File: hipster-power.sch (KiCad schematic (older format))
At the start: 16 parts, among them SW3 ON|OFF, U3 NCP5501, U4 MCP73831

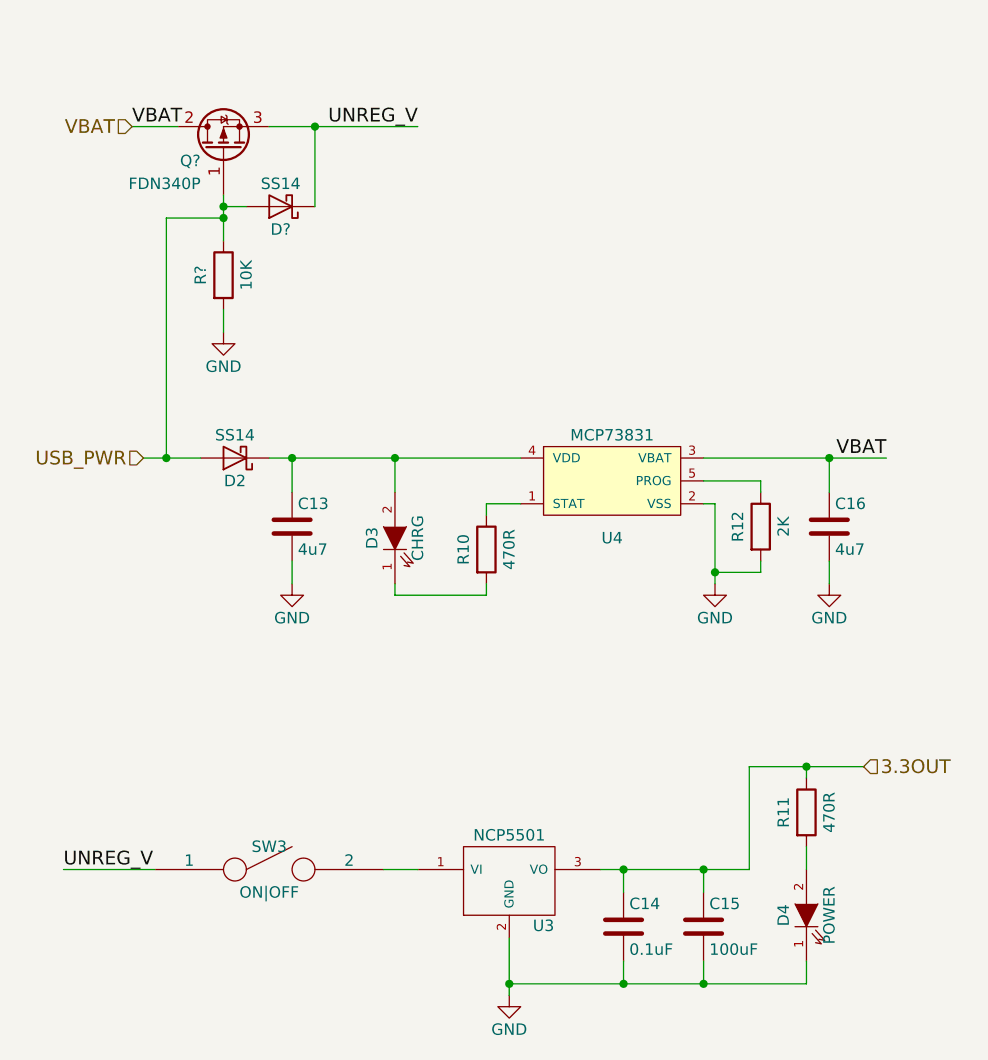
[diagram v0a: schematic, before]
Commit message: Remove power LED
Will reduce deep sleep power consumption to 1% or less of previous.

Ref #6.
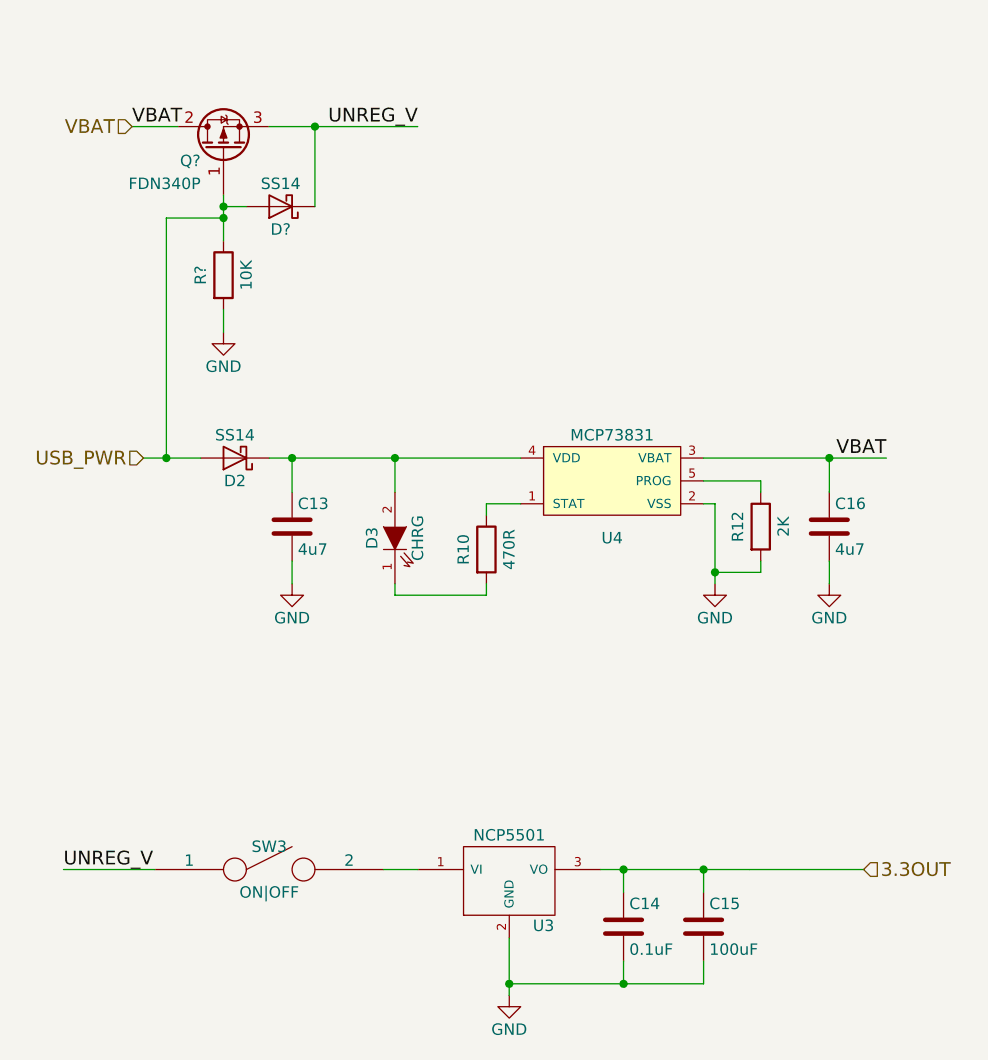
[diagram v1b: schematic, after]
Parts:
- removed D4: POWER, symbol LED-RESCUE-minimum-viable-badge
- removed R11: 470R, symbol R
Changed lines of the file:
@@
-$EndComp
-$Comp
-L LED-RESCUE-minimum-viable-badge D4
-U 1 1 59287320
-P 5200 4550
-AR Path="/59287320" Ref="D4"  Part="1"
-AR Path="/592826E7/59287320" Ref="D4"  Part="1"
-F 0 "D4" H 5200 4650 50  0000 C CNN
-F 1 "POWER" H 5200 4450 50  0000 C CNN
-F 2 "" H 5200 4550 50  0001 C CNN
-F 3 "" H 5200 4550 50  0000 C CNN
-	1    5200 4550
-	0    -1   -1   0
-$EndComp
-$Comp
-L R R11
-U 1 1 59287729
-P 5200 4100
-F 0 "R11" V 5100 4100 50  0000 C CNN
-F 1 "470R" V 5300 4100 50  0000 C CNN
-F 2 "" V 5130 4100 50  0001 C CNN
-F 3 "" H 5200 4100 50  0000 C CNN
-	1    5200 4100
-	1    0    0    -1
 $EndComp
 $Comp
@@
 	1    0    0    -1
 $EndComp
-Text HLabel 5450 3900 2    60   Input ~ 0
+Text HLabel 5450 4350 2    60   Input ~ 0
 3.3OUT
 $Comp
@@
 $EndComp
 Wire Wire Line
-	2300 2550 2550 2550
+	2300 2550 2400 2550
+Wire Wire Line
+	2400 2550 2550 2550
 Wire Wire Line
 	2950 3100 2950 3000
@@
 	3350 4350 3500 4350
 Wire Wire Line
-	5200 4350 5200 4250
-Wire Wire Line
-	4300 4350 4950 4350
-Wire Wire Line
-	4950 4350 4950 3900
-Wire Wire Line
-	4950 3900 5450 3900
-Wire Wire Line
-	5200 3900 5200 3950
+	4300 4350 4400 4350
+Wire Wire Line
+	4400 4350 4750 4350
+Wire Wire Line
+	4750 4350 4950 4350
+Wire Wire Line
+	4950 4350 4950 4350
+Wire Wire Line
+	4950 4350 5450 4350
 Wire Wire Line
 	4750 4450 4750 4350
@@
 Connection ~ 4400 4350
 Wire Wire Line
-	3900 4650 3900 4900
-Wire Wire Line
-	3900 4850 5200 4850
+	3900 4650 3900 4850
+Wire Wire Line
+	3900 4850 3900 4900
 Wire Wire Line
 	4400 4850 4400 4750
@@
 	4750 4850 4750 4750
 Connection ~ 4400 4850
-Wire Wire Line
-	5200 4850 5200 4750
-Connection ~ 4750 4850
 Connection ~ 3900 4850
-Connection ~ 5200 3900
-Wire Wire Line
-	2850 2550 3950 2550
+Wire Wire Line
+	2850 2550 2950 2550
+Wire Wire Line
+	2950 2550 3400 2550
+Wire Wire Line
+	3400 2550 3950 2550
 Wire Wire Line
 	3400 2700 3400 2550
@@
 	4750 2750 4800 2750
 Wire Wire Line
-	4800 2750 4800 3100
+	4800 2750 4800 3050
+Wire Wire Line
+	4800 3050 4800 3100
 Wire Wire Line
 	4800 3050 5000 3050
@@
 	5300 3100 5300 3000
 Wire Wire Line
-	4750 2550 5550 2550
+	4750 2550 5300 2550
+Wire Wire Line
+	5300 2550 5550 2550
 Wire Wire Line
 	5300 2550 5300 2700
@@
 	2250 1100 2450 1100
 Wire Wire Line
-	2850 1100 3500 1100
-Wire Wire Line
-	2650 1400 2650 1600
+	2850 1100 3050 1100
+Wire Wire Line
+	3050 1100 3500 1100
+Wire Wire Line
+	2650 1400 2650 1450
+Wire Wire Line
+	2650 1450 2650 1500
+Wire Wire Line
+	2650 1500 2650 1600
 Wire Wire Line
 	3050 1450 3050 1100
@@
 Wire Wire Line
 	2400 1500 2400 2550
+Wire Wire Line
+	4750 4850 4400 4850
+Wire Wire Line
+	4400 4850 3900 4850
 $EndSCHEMATC

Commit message: Arrange & label schematic, pass ERC
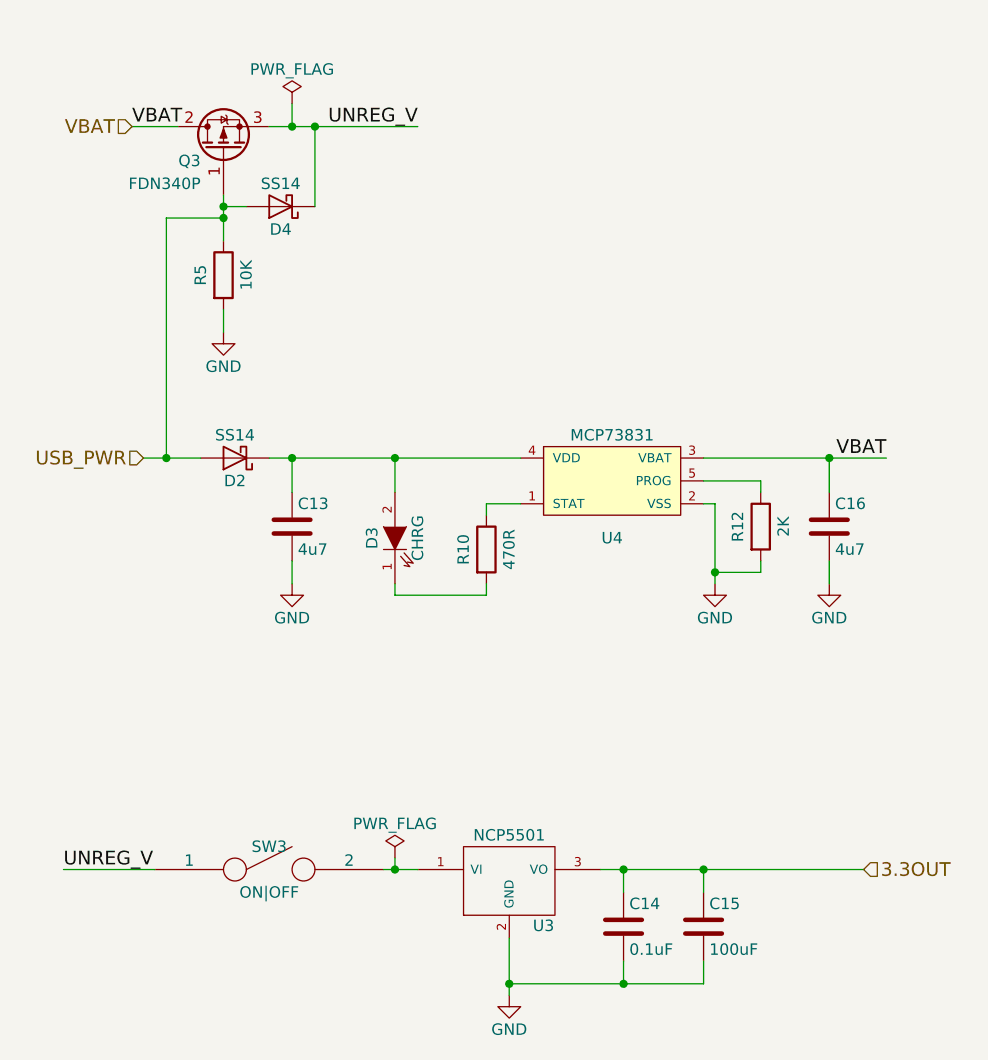
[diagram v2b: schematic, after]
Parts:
- gave numbers to parts that had none: 3
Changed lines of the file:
@@
 $Descr A4 11693 8268
 encoding utf-8
-Sheet 2 2
+Sheet 2 3
 Title ""
 Date ""
@@
 $EndComp
 $Comp
-L GND #PWR21
+L GND #PWR020
 U 1 1 592830E1
 P 2950 3100
-F 0 "#PWR21" H 2950 2850 50  0001 C CNN
+F 0 "#PWR020" H 2950 2850 50  0001 C CNN
 F 1 "GND" H 2950 2950 50  0000 C CNN
 F 2 "" H 2950 3100 50  0000 C CNN
@@
 $EndComp
 $Comp
-L GND #PWR22
+L GND #PWR021
 U 1 1 59287D1C
 P 3900 4900
-F 0 "#PWR22" H 3900 4650 50  0001 C CNN
+F 0 "#PWR021" H 3900 4650 50  0001 C CNN
 F 1 "GND" H 3900 4750 50  0000 C CNN
 F 2 "" H 3900 4900 50  0000 C CNN
@@
 $EndComp
 $Comp
-L GND #PWR23
+L GND #PWR022
 U 1 1 59358631
 P 4800 3100
-F 0 "#PWR23" H 4800 2850 50  0001 C CNN
+F 0 "#PWR022" H 4800 2850 50  0001 C CNN
 F 1 "GND" H 4800 2950 50  0000 C CNN
 F 2 "" H 4800 3100 50  0000 C CNN
@@
 $EndComp
 $Comp
-L GND #PWR24
+L GND #PWR023
 U 1 1 5935870E
 P 5300 3100
-F 0 "#PWR24" H 5300 2850 50  0001 C CNN
+F 0 "#PWR023" H 5300 2850 50  0001 C CNN
 F 1 "GND" H 5300 2950 50  0000 C CNN
 F 2 "" H 5300 3100 50  0000 C CNN
@@
 VBAT
 $Comp
-L D_Schottky D?
+L D_Schottky D4
 U 1 1 59A10ECB
 P 2900 1450
-F 0 "D?" H 2900 1550 50  0000 C CNN
+F 0 "D4" H 2900 1550 50  0000 C CNN
 F 1 "SS14" H 2900 1350 50  0000 C CNN
 F 2 "Diodes_SMD:D_SMA" H 2900 1450 50  0001 C CNN
@@
 $EndComp
 $Comp
-L GND #PWR?
+L GND #PWR024
 U 1 1 59A1135B
 P 2650 2000
-F 0 "#PWR?" H 2650 1750 50  0001 C CNN
+F 0 "#PWR024" H 2650 1750 50  0001 C CNN
 F 1 "GND" H 2650 1850 50  0000 C CNN
 F 2 "" H 2650 2000 50  0000 C CNN
@@
 $EndComp
 $Comp
-L R R?
+L R R5
 U 1 1 59A11654
 P 2650 1750
-F 0 "R?" V 2550 1750 50  0000 C CNN
+F 0 "R5" V 2550 1750 50  0000 C CNN
 F 1 "10K" V 2750 1750 50  0000 C CNN
 F 2 "" V 2580 1750 50  0001 C CNN
@@
 VBAT
 $Comp
-L Q_PMOS_GDS Q?
+L Q_PMOS_GDS Q3
 U 1 1 59A3FE7A
 P 2650 1200
-F 0 "Q?" V 2600 1300 50  0000 L CNN
+F 0 "Q3" V 2600 1300 50  0000 L CNN
 F 1 "FDN340P" V 2500 1300 50  0000 L CNN
 F 2 "" H 2850 1300 50  0001 C CNN
@@
 $EndComp
 Wire Wire Line
-	2300 2550 2400 2550
-Wire Wire Line
-	2400 2550 2550 2550
+	2300 2550 2550 2550
 Wire Wire Line
 	2950 3100 2950 3000
@@
 	3350 4350 3500 4350
 Wire Wire Line
-	4300 4350 4400 4350
-Wire Wire Line
-	4400 4350 4750 4350
-Wire Wire Line
-	4750 4350 4950 4350
-Wire Wire Line
-	4950 4350 4950 4350
-Wire Wire Line
-	4950 4350 5450 4350
+	4300 4350 5450 4350
 Wire Wire Line
 	4750 4450 4750 4350
@@
 Connection ~ 4400 4350
 Wire Wire Line
-	3900 4650 3900 4850
-Wire Wire Line
-	3900 4850 3900 4900
+	3900 4650 3900 4900
 Wire Wire Line
 	4400 4850 4400 4750
@@
 Connection ~ 3900 4850
 Wire Wire Line
-	2850 2550 2950 2550
-Wire Wire Line
-	2950 2550 3400 2550
-Wire Wire Line
-	3400 2550 3950 2550
+	2850 2550 3950 2550
 Wire Wire Line
 	3400 2700 3400 2550
@@
 	4750 2750 4800 2750
 Wire Wire Line
-	4800 2750 4800 3050
-Wire Wire Line
-	4800 3050 4800 3100
+	4800 2750 4800 3100
 Wire Wire Line
 	4800 3050 5000 3050
@@
 	5300 3100 5300 3000
 Wire Wire Line
-	4750 2550 5300 2550
-Wire Wire Line
-	5300 2550 5550 2550
+	4750 2550 5550 2550
 Wire Wire Line
 	5300 2550 5300 2700
@@
 	2250 1100 2450 1100
 Wire Wire Line
-	2850 1100 3050 1100
-Wire Wire Line
-	3050 1100 3500 1100
-Wire Wire Line
-	2650 1400 2650 1450
-Wire Wire Line
-	2650 1450 2650 1500
-Wire Wire Line
-	2650 1500 2650 1600
+	2850 1100 3500 1100
+Wire Wire Line
+	2650 1400 2650 1600
 Wire Wire Line
 	3050 1450 3050 1100
@@
 	2400 1500 2400 2550
 Wire Wire Line
-	4750 4850 4400 4850
-Wire Wire Line
-	4400 4850 3900 4850
+	3900 4850 4750 4850
+$Comp
+L PWR_FLAG #FLG025
+U 1 1 59A7D662
+P 3400 4300
+F 0 "#FLG025" H 3400 4375 50  0001 C CNN
+F 1 "PWR_FLAG" H 3400 4450 50  0000 C CNN
+F 2 "" H 3400 4300 50  0001 C CNN
+F 3 "" H 3400 4300 50  0001 C CNN
+	1    3400 4300
+	1    0    0    -1
+$EndComp
+Wire Wire Line
+	3400 4300 3400 4350
+Connection ~ 3400 4350
+$Comp
+L PWR_FLAG #FLG026
+U 1 1 59A7D985
+P 2950 1000
+F 0 "#FLG026" H 2950 1075 50  0001 C CNN
+F 1 "PWR_FLAG" H 2950 1150 50  0000 C CNN
+F 2 "" H 2950 1000 50  0001 C CNN
+F 3 "" H 2950 1000 50  0001 C CNN
+	1    2950 1000
+	1    0    0    -1
+$EndComp
+Wire Wire Line
+	2950 1000 2950 1100
+Connection ~ 2950 1100
 $EndSCHEMATC

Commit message: Add e-ink gate drive circuitry
Closes #14
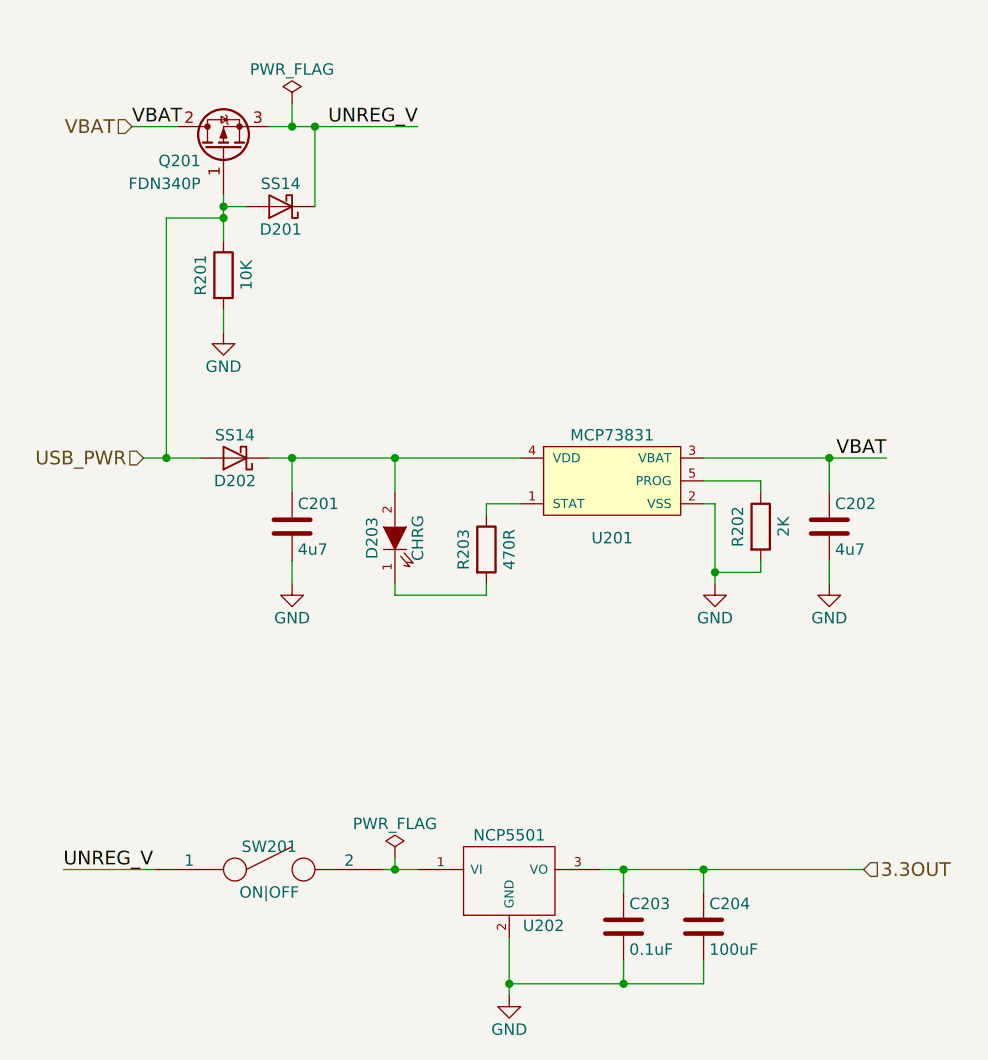
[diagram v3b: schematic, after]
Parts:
- renumbered C13 to C201, C16 to C202, C14 to C203, C15 to C204, D4 to D201, D2 to D202, D3 to D203, Q3 to Q201, R5 to R201, R12 to R202, R10 to R203, SW3 to SW201, U4 to U201, U3 to U202
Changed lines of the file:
@@
 USB_PWR
 $Comp
-L R R10
+L R R203
 U 1 1 59282A8D
 P 3800 2950
-F 0 "R10" V 3700 2950 50  0000 C CNN
+F 0 "R203" V 3700 2950 50  0000 C CNN
 F 1 "470R" V 3900 2950 50  0000 C CNN
 F 2 "Resistors_SMD:R_0603_HandSoldering" V 3730 2950 50  0001 C CNN
@@
 $EndComp
 $Comp
-L LED-RESCUE-minimum-viable-badge D3
+L LED-RESCUE-minimum-viable-badge D203
 U 1 1 59282B08
 P 3400 2900
-AR Path="/59282B08" Ref="D3"  Part="1"
-AR Path="/592826E7/59282B08" Ref="D3"  Part="1"
-F 0 "D3" H 3400 3000 50  0000 C CNN
+F 0 "D203" H 3400 3000 50  0000 C CNN
 F 1 "CHRG" H 3400 2800 50  0000 C CNN
 F 2 "LEDs:LED_0603" H 3400 2900 50  0001 C CNN
@@
 $EndComp
 $Comp
-L C C13
+L C C201
 U 1 1 59282FCC
 P 2950 2850
-F 0 "C13" H 2975 2950 50  0000 L CNN
+F 0 "C201" H 2975 2950 50  0000 L CNN
 F 1 "4u7" H 2975 2750 50  0000 L CNN
 F 2 "Capacitors_SMD:C_0805_HandSoldering" H 2988 2700 50  0001 C CNN
@@
 $EndComp
 $Comp
-L R R12
+L R R202
 U 1 1 592833D5
 P 5000 2850
-F 0 "R12" V 4900 2850 50  0000 C CNN
+F 0 "R202" V 4900 2850 50  0000 C CNN
 F 1 "2K" V 5100 2850 50  0000 C CNN
 F 2 "Resistors_SMD:R_0603_HandSoldering" V 4930 2850 50  0001 C CNN
@@
 UNREG_V
 $Comp
-L SPST SW3
+L SPST SW201
 U 1 1 59286658
 P 2850 4350
-F 0 "SW3" H 2850 4450 50  0000 C CNN
+F 0 "SW201" H 2850 4450 50  0000 C CNN
 F 1 "ON|OFF" H 2850 4250 50  0000 C CNN
 F 2 "libs:SS12D00" H 2850 4350 50  0001 C CNN
@@
 UNREG_V
 $Comp
-L NCP5501 U3
+L NCP5501 U202
 U 1 1 59286CBF
 P 3900 4400
-F 0 "U3" H 4050 4204 50  0000 C CNN
+F 0 "U202" H 4050 4204 50  0000 C CNN
 F 1 "NCP5501" H 3900 4600 50  0000 C CNN
 F 2 "libs:DPAK3.NCP5501" H 3900 4400 50  0001 C CNN
@@
 $EndComp
 $Comp
-L C C14
+L C C203
 U 1 1 59287000
 P 4400 4600
-F 0 "C14" H 4425 4700 50  0000 L CNN
+F 0 "C203" H 4425 4700 50  0000 L CNN
 F 1 "0.1uF" H 4425 4500 50  0000 L CNN
 F 2 "Capacitors_SMD:C_0603_HandSoldering" H 4438 4450 50  0001 C CNN
@@
 $EndComp
 $Comp
-L C C15
+L C C204
 U 1 1 592871C6
 P 4750 4600
-F 0 "C15" H 4775 4700 50  0000 L CNN
+F 0 "C204" H 4775 4700 50  0000 L CNN
 F 1 "100uF" H 4775 4500 50  0000 L CNN
 F 2 "Capacitors_SMD:C_1210_HandSoldering" H 4788 4450 50  0001 C CNN
@@
 3.3OUT
 $Comp
-L MCP73831 U4
+L MCP73831 U201
 U 1 1 5935729B
 P 4350 2650
-F 0 "U4" H 4350 2400 50  0000 C CNN
+F 0 "U201" H 4350 2400 50  0000 C CNN
 F 1 "MCP73831" H 4350 2850 50  0000 C CNN
 F 2 "TO_SOT_Packages_SMD:SOT-23-5_HandSoldering" H 4350 2650 60  0001 C CNN
@@
 $EndComp
 $Comp
-L C C16
+L C C202
 U 1 1 59358708
 P 5300 2850
-F 0 "C16" H 5325 2950 50  0000 L CNN
+F 0 "C202" H 5325 2950 50  0000 L CNN
 F 1 "4u7" H 5325 2750 50  0000 L CNN
 F 2 "Capacitors_SMD:C_0805_HandSoldering" H 5338 2700 50  0001 C CNN
@@
 VBAT
 $Comp
-L D_Schottky D4
+L D_Schottky D201
 U 1 1 59A10ECB
 P 2900 1450
-F 0 "D4" H 2900 1550 50  0000 C CNN
+F 0 "D201" H 2900 1550 50  0000 C CNN
 F 1 "SS14" H 2900 1350 50  0000 C CNN
 F 2 "Diodes_SMD:D_SMA" H 2900 1450 50  0001 C CNN
@@
 $EndComp
 $Comp
-L R R5
+L R R201
 U 1 1 59A11654
 P 2650 1750
-F 0 "R5" V 2550 1750 50  0000 C CNN
+F 0 "R201" V 2550 1750 50  0000 C CNN
 F 1 "10K" V 2750 1750 50  0000 C CNN
 F 2 "" V 2580 1750 50  0001 C CNN
@@
 VBAT
 $Comp
-L Q_PMOS_GDS Q3
+L Q_PMOS_GDS Q201
 U 1 1 59A3FE7A
 P 2650 1200
-F 0 "Q3" V 2600 1300 50  0000 L CNN
+F 0 "Q201" V 2600 1300 50  0000 L CNN
 F 1 "FDN340P" V 2500 1300 50  0000 L CNN
 F 2 "" H 2850 1300 50  0001 C CNN
@@
 Connection ~ 2650 1450
 $Comp
-L D_Schottky D2
+L D_Schottky D202
 U 1 1 592829A1
 P 2700 2550
-F 0 "D2" H 2700 2650 50  0000 C CNN
+F 0 "D202" H 2700 2650 50  0000 C CNN
 F 1 "SS14" H 2700 2450 50  0000 C CNN
 F 2 "Diodes_SMD:D_SMA" H 2700 2550 50  0001 C CNN

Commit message: Set component footprints.
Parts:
- Q201: footprint (none) -> libs:SOT23_FET
- R201: footprint (none) -> Resistors_SMD:R_0603_HandSoldering
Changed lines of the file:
@@
 F 0 "R201" V 2550 1750 50  0000 C CNN
 F 1 "10K" V 2750 1750 50  0000 C CNN
-F 2 "" V 2580 1750 50  0001 C CNN
+F 2 "Resistors_SMD:R_0603_HandSoldering" V 2580 1750 50  0001 C CNN
 F 3 "" H 2650 1750 50  0000 C CNN
 	1    2650 1750
@@
 F 0 "Q201" V 2600 1300 50  0000 L CNN
 F 1 "FDN340P" V 2500 1300 50  0000 L CNN
-F 2 "" H 2850 1300 50  0001 C CNN
+F 2 "libs:SOT23_FET" H 2850 1300 50  0001 C CNN
 F 3 "" H 2650 1200 50  0001 C CNN
 	1    2650 1200

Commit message: Placement started
Predicting Bob will end up changing all this
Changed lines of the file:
@@
 LIBS:NCP5501
 LIBS:mcp73831
+LIBS:q_pmos_gds
 LIBS:minimum-viable-badge-cache
 EELAYER 25 0
@@
 Text Label 5550 2550 2    60   ~ 0
 VBAT
-$Comp
-L Q_PMOS_GDS Q201
-U 1 1 59A3FE7A
-P 2650 1200
-F 0 "Q201" V 2600 1300 50  0000 L CNN
-F 1 "FDN340P" V 2500 1300 50  0000 L CNN
-F 2 "libs:SOT23_FET" H 2850 1300 50  0001 C CNN
-F 3 "" H 2650 1200 50  0001 C CNN
-	1    2650 1200
-	0    -1   -1   0
-$EndComp
 Wire Wire Line
 	2300 2550 2550 2550
@@
 	2950 1000 2950 1100
 Connection ~ 2950 1100
+$Comp
+L Q_PMOS_GDS Q201
+U 1 1 59AAE4B9
+P 2650 1200
+F 0 "Q201" H 2850 1250 50  0000 L CNN
+F 1 "FDN340P" H 2850 1150 50  0000 L CNN
+F 2 "libs:SOT23_FET" H 2850 1300 50  0001 C CNN
+F 3 "" H 2650 1200 50  0001 C CNN
+	1    2650 1200
+	0    -1   -1   0
+$EndComp
 $EndSCHEMATC

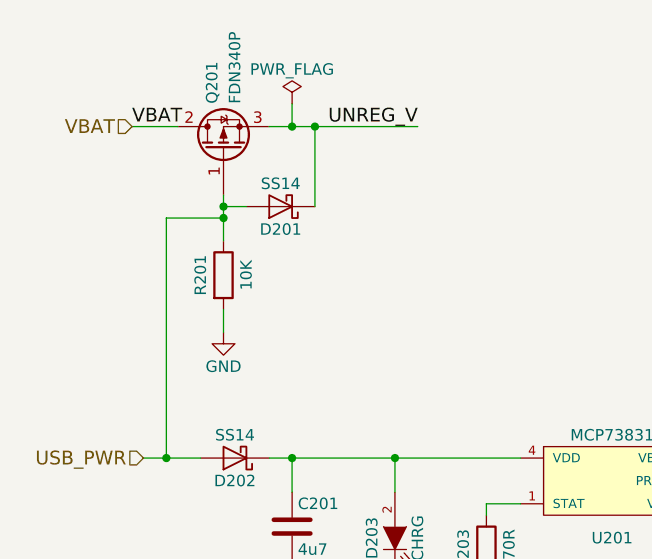
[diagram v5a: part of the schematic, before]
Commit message: Minor updates to schematic components.
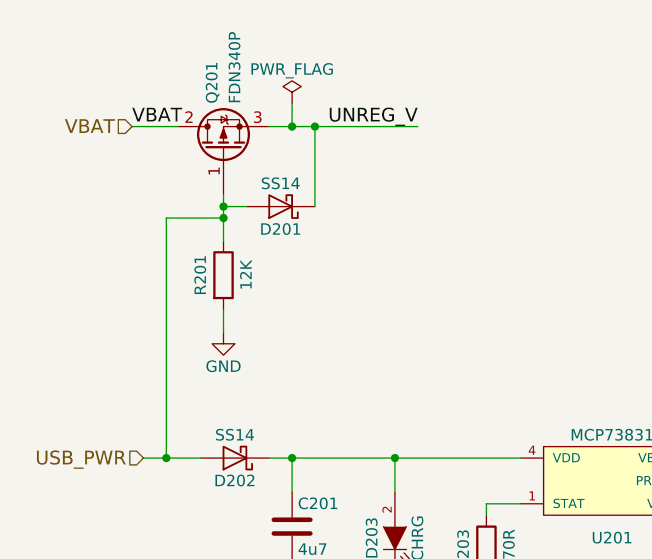
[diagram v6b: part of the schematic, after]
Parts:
- R201: value 10K -> 12K
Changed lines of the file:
@@
 P 2650 1750
 F 0 "R201" V 2550 1750 50  0000 C CNN
-F 1 "10K" V 2750 1750 50  0000 C CNN
+F 1 "12K" V 2750 1750 50  0000 C CNN
 F 2 "Resistors_SMD:R_0603_HandSoldering" V 2580 1750 50  0001 C CNN
 F 3 "" H 2650 1750 50  0000 C CNN
